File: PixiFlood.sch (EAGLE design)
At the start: 62 parts, among them IC1 L78LXXCU/BU, IC2 74LVC1G125DBV, IC3 LM1117-SOT223, IC4 WS2811SOP8, IC5 TC7W04FP-0.65, U1 PT4115B89E, U2 PT4115B89E, U3 PT4115B89E, X1 22-23-2041

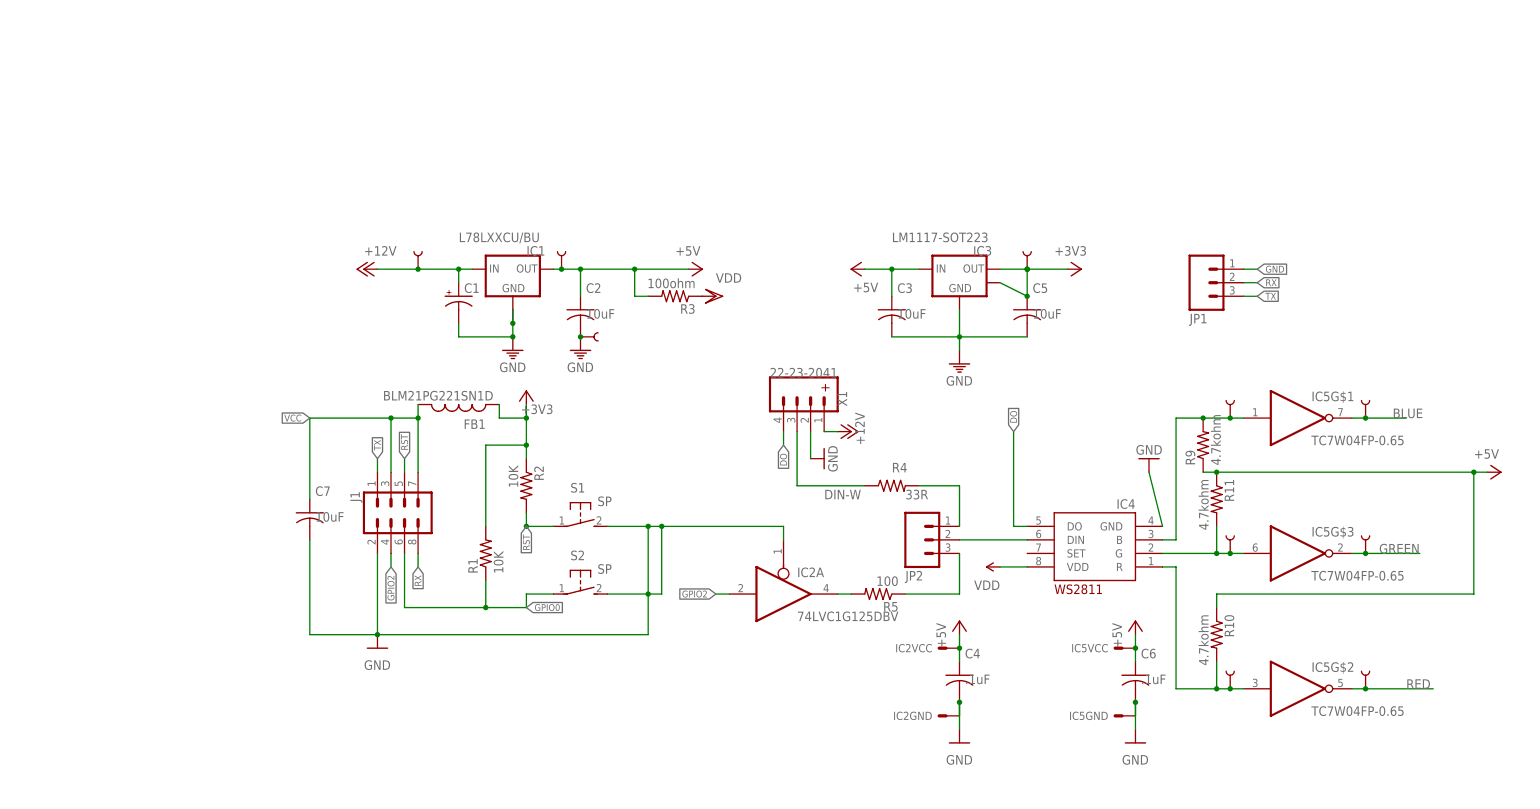
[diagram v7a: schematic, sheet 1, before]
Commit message: Reworked layout
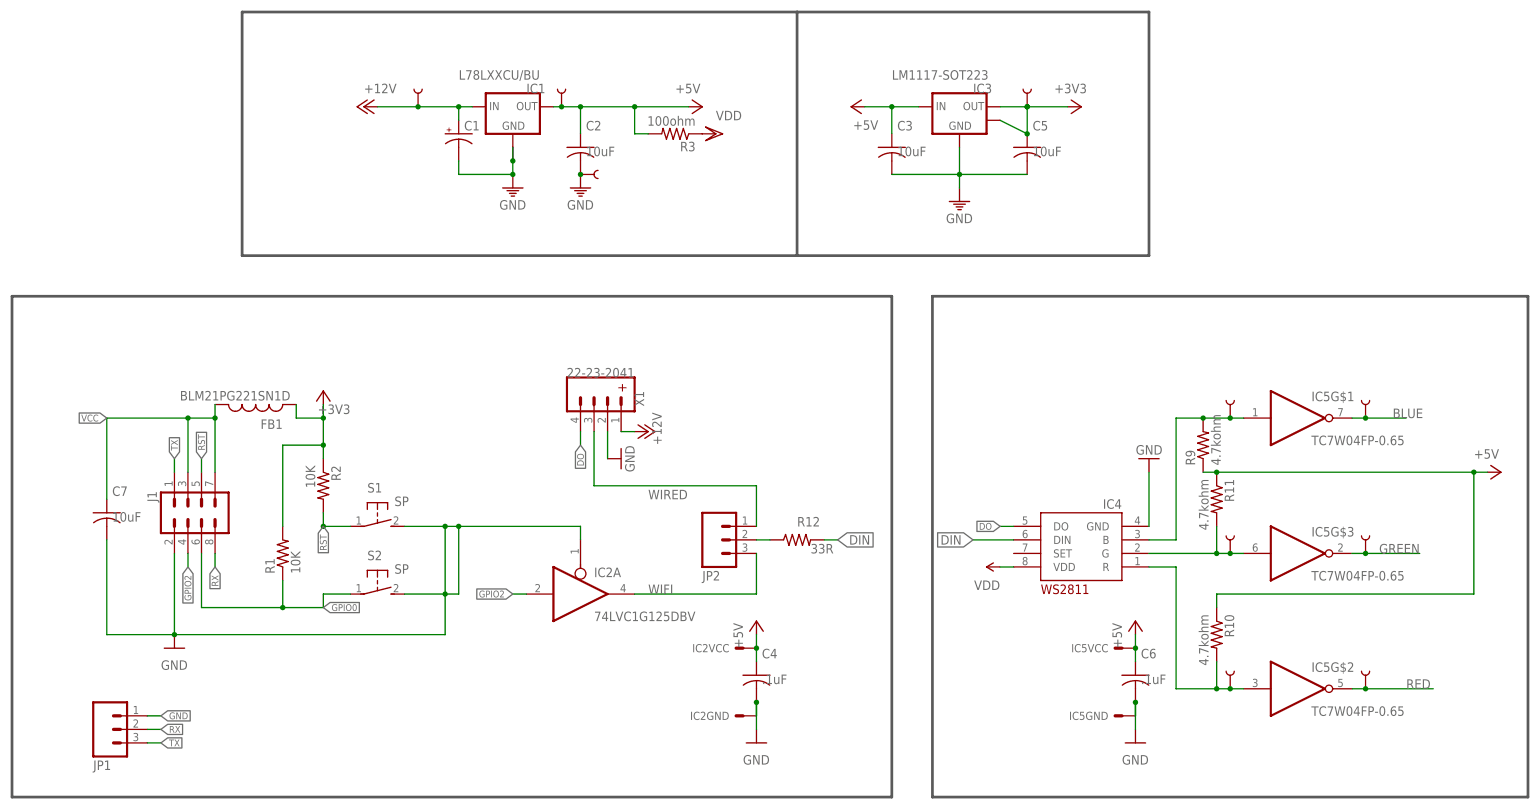
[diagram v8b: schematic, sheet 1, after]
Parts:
- removed R4: 33R, rcl:R-US_M1206
- removed R5: 100, resistors:R-US_R0805
- removed TP26, TP27, TP28, TP29, TP30, TP31: TEST-POINTTP_15TH_THRU, SparkFun-Connectors:TEST-POINTTP_15TH_THRU
- added R12: 33R, rcl:R-US_M1206
- TP1, TP10, TP17, TP18, TP19, TP2, TP20, TP21, TP22, TP23, TP24, TP25, TP3: value TEST-POINTTP_15TH_THRU -> TEST_PINTP-1; device SparkFun-Connectors:TEST-POINTTP_15TH_THRU -> connectors:TEST_PINTP-1
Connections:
- removed net DIN-W: R4.1, X1.3
- removed net N$6: IC2A.O, R5.2
- new net N$7: JP2.2, R12.1
- net BOUT: no longer TP30.1
- net DIN: now also R12.2; no longer JP2.2
- net GOUT: no longer TP29.1
- net LED-B-NEG: no longer TP31.1
- net LED-G-NEG: no longer TP28.1
- net LED-R-NEG: no longer TP27.1
- net ROUT: no longer TP26.1
- net WIFI: now also IC2A.O; no longer R5.1
- net WIRED: now also X1.3; no longer R4.2
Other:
- moved on the sheet: C1, C2, C3, C4, C5, C7, FB1, IC1, IC2A, IC2GND, IC2VCC, IC3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
